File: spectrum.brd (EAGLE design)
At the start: 100 x 28.2 mm, 38 parts, among them CN1 PH-1X06RG, CN2 PH-1X04SG, CN3 PH-1X04SG, CN4 FH-1X06RG, IC1 7W14FU, IC2 7W14FU, IC3 7W14FU, IC5 NJM2670E3, IC6 NJM2670E3, IC7 NJM2670E3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

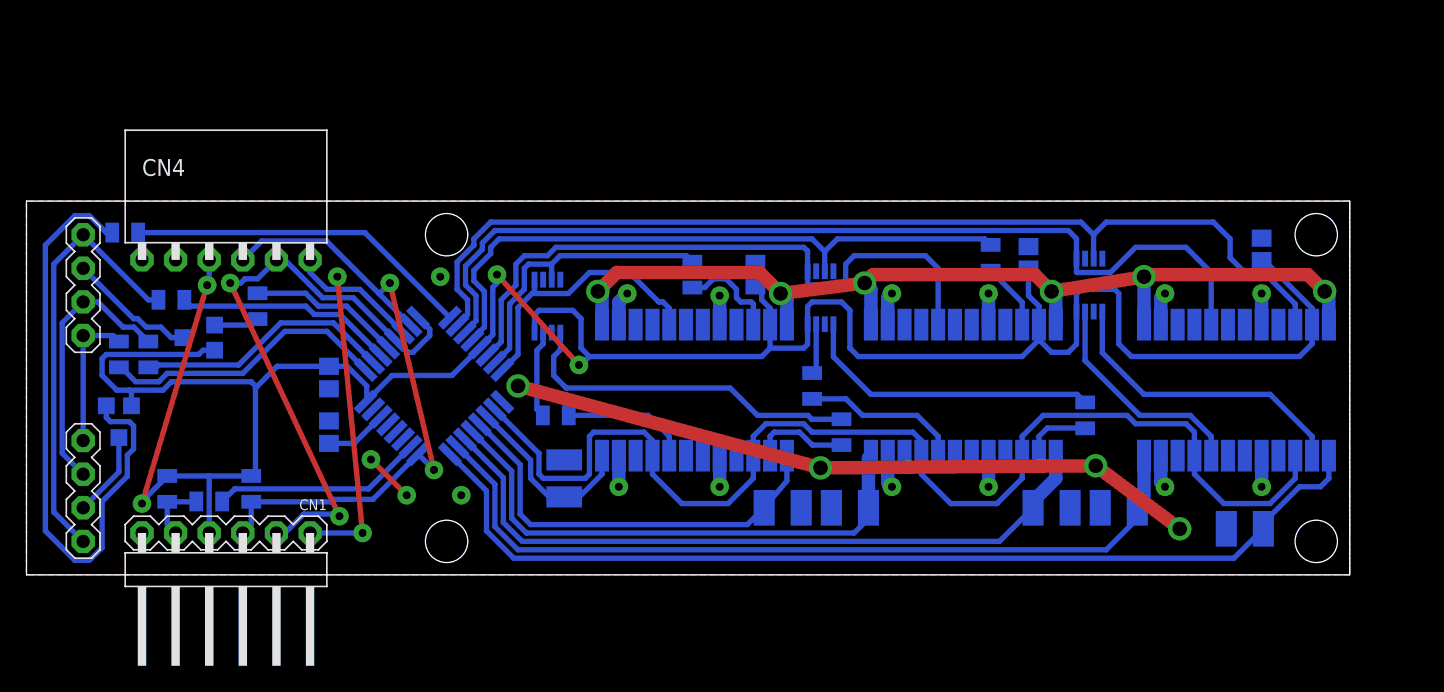
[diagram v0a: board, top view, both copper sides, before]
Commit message: Added power chains
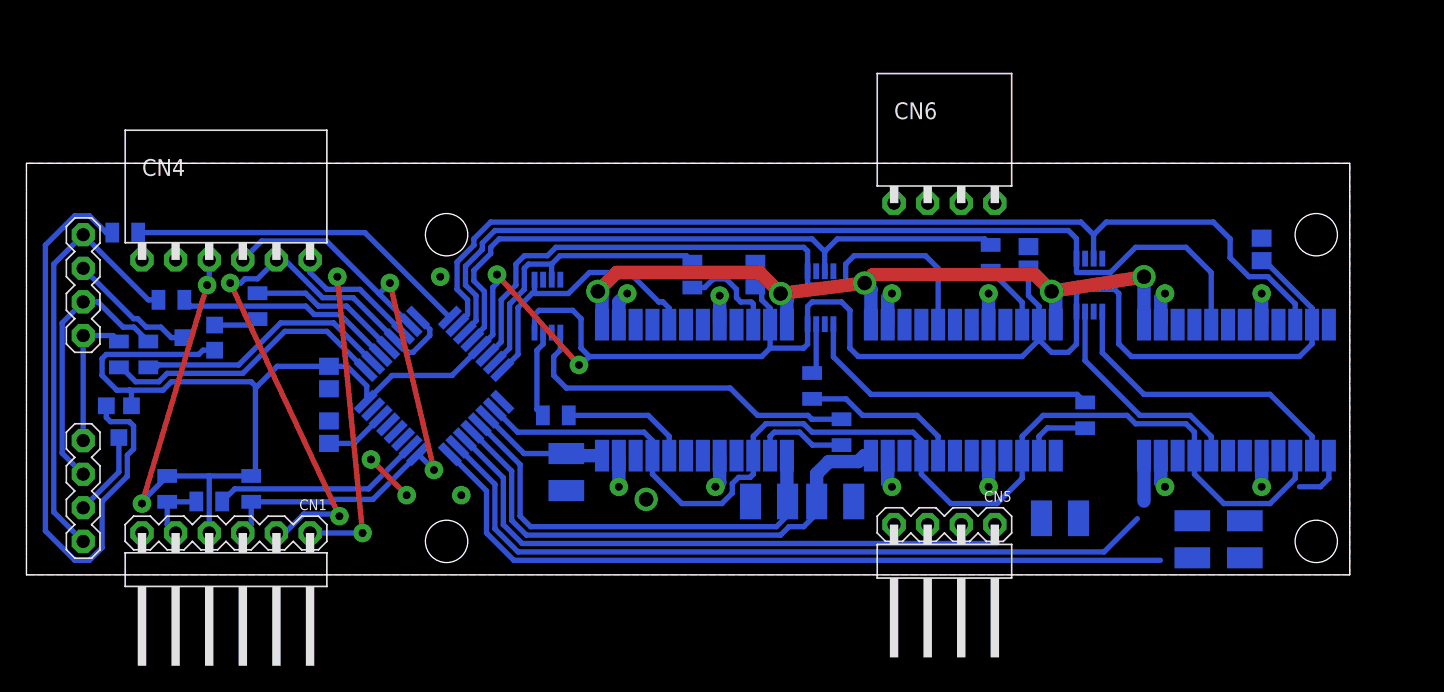
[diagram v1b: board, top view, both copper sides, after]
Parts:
- added CN5: PH-1X04SGRG, MyLib:PH-1X04RG
- added CN6: FH-1X04RG, MyLib:FH-1X04RG
- moved R2 6.05 mm to (88.1, 2.70), turned to 90 degrees
- moved R4 1.21 mm to (61.1, 5.56), turned to 0 degrees
- moved R5 1.14 mm to (56.1, 5.56), turned to 180 degrees
- moved R3 1.02 mm to (78.1, 4.29), turned to 180 degrees
- moved R1 0.79 mm to (92.1, 2.70), turned to 90 degrees
- moved R6 0.50 mm to (40.8, 7.78), turned to 90 degrees
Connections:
- new net N$42: CN5.3, CN6.2
- new net N$43: CN5.2, CN6.3
- new net N$45: CN5.1, CN6.4
- new net N$46: CN5.4, CN6.1
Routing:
- net GND: track 56.2 -> 3.82 mm, vias 8 -> 5
- net N$13: track 75.1 -> 58.5 mm, vias 6 -> 5
- net N$1: track 75.9 -> 63.1 mm
- net N$5: track 53.8 -> 45.6 mm
- net N$10: track 90.5 -> 85.3 mm
- net N$8: track 14.1 -> 9.88 mm
- net N$2: track 62.4 -> 61.1 mm
- net N$6: track 40.7 -> 39.8 mm
- net N$9: track 33.1 -> 33.6 mm
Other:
- board size 100 x 28.2 mm -> 100 x 31.1 mm

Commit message: Complete routing for the first time
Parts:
- added C6: 1500u, MyLib:E3,5-8
- added R21, R22, R23, R24, R25: 0, MyLib:0204/7
- added R26: 0, MyLib:0204/5
- R20: device MyLib:R2012 -> MyLib:0204/5
- moved R20 33.5 mm to (47.3, 5.87), flipped to the top, turned to 270 degrees
- moved R19 13.4 mm to (20.0, 19.7), turned to 0 degrees
- moved R17 13.1 mm to (22.4, 27.1)
- moved R8 12.6 mm to (20.2, 14.8)
- moved CN4 12.4 mm to (24.8, 31.6)
- moved Q2 12.0 mm to (23.2, 24.3)
- moved R18 11.9 mm to (20.0, 21.7), turned to 0 degrees
- moved R15 11.3 mm to (26.5, 27.1), turned to 0 degrees
- moved CN2 10.6 mm to (14.3, 25.4)
- moved CN3 10.6 mm to (14.3, 9.84)
- moved CN1 10.5 mm to (24.8, 7.30)
- moved Q1 10.2 mm to (16.4, 15.7)
- moved R16 9.60 mm to (15.4, 31.3)
- moved R7 5.85 mm to (21.4, 10.3), turned to 90 degrees
- moved CN5 5.40 mm to (69.4, 7.30)
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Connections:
- removed net N$44: IC8.2, R20.2
- new net N$47: IC7.13, R25.1
- net GND: now also C6.-, CN5.2, CN5.3, CN6.2, CN6.3, R20.1, R20.2, R26.1, R26.2
- net N$13: now also C6.+, CN5.1, CN5.4, CN6.1, CN6.4, R21.1, R22.2, R23.2, R24.2, R25.2; no longer IC5.13, IC6.13, IC6.24, IC7.13, IC7.24
- net N$42: now also IC5.13, R21.2; no longer CN5.3, CN6.2
- net N$43: now also IC6.24, R22.1; no longer CN5.2, CN6.3
- net N$45: now also IC6.13, R23.1; no longer CN5.1, CN6.4
- net N$46: now also IC7.24, R24.1; no longer CN5.4, CN6.1
- net RESET: now also IC8.2; no longer R20.1
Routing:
- net N$13: track 58.5 -> 126.2 mm, vias 5 -> 4
- net +5V: track 199.4 -> 177.0 mm
- net N$5: track 45.6 -> 64.6 mm
- net N$41: track 22.0 -> 4.95 mm
- net N$44: track 16.0 -> 0.00 mm
- net N$40: track 19.6 -> 6.13 mm
- net RESET: track 4.83 -> 17.4 mm
- net N$1: track 63.1 -> 75.1 mm
- net N$2: track 61.1 -> 68.4 mm
- net N$19: track 45.8 -> 39.1 mm
- net TOOL0: track 50.0 -> 54.2 mm
- net N$36: track 11.6 -> 7.48 mm
- net N$32: track 16.6 -> 12.7 mm
- net GND: track 3.82 -> 0.00 mm, vias 5 -> 2
- net N$4: track 71.8 -> 68.4 mm
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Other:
- board size 100 x 31.1 mm -> 92.2 x 33.2 mm
